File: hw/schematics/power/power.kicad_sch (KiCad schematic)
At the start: 16 parts

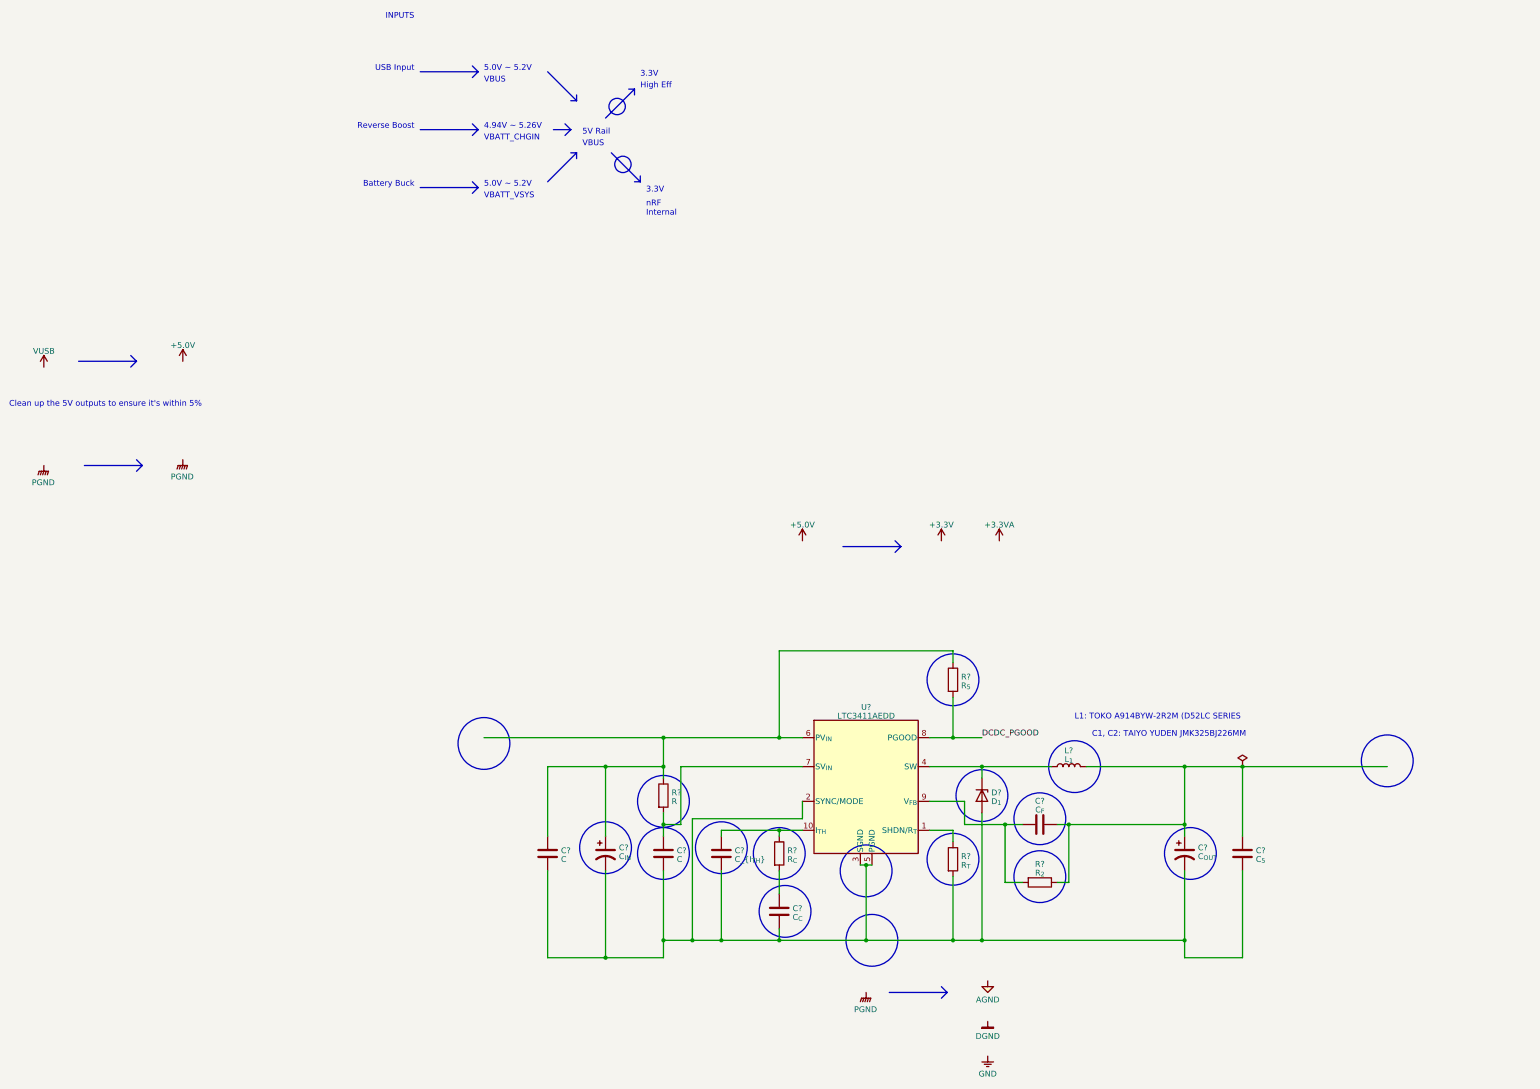
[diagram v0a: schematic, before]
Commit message: 
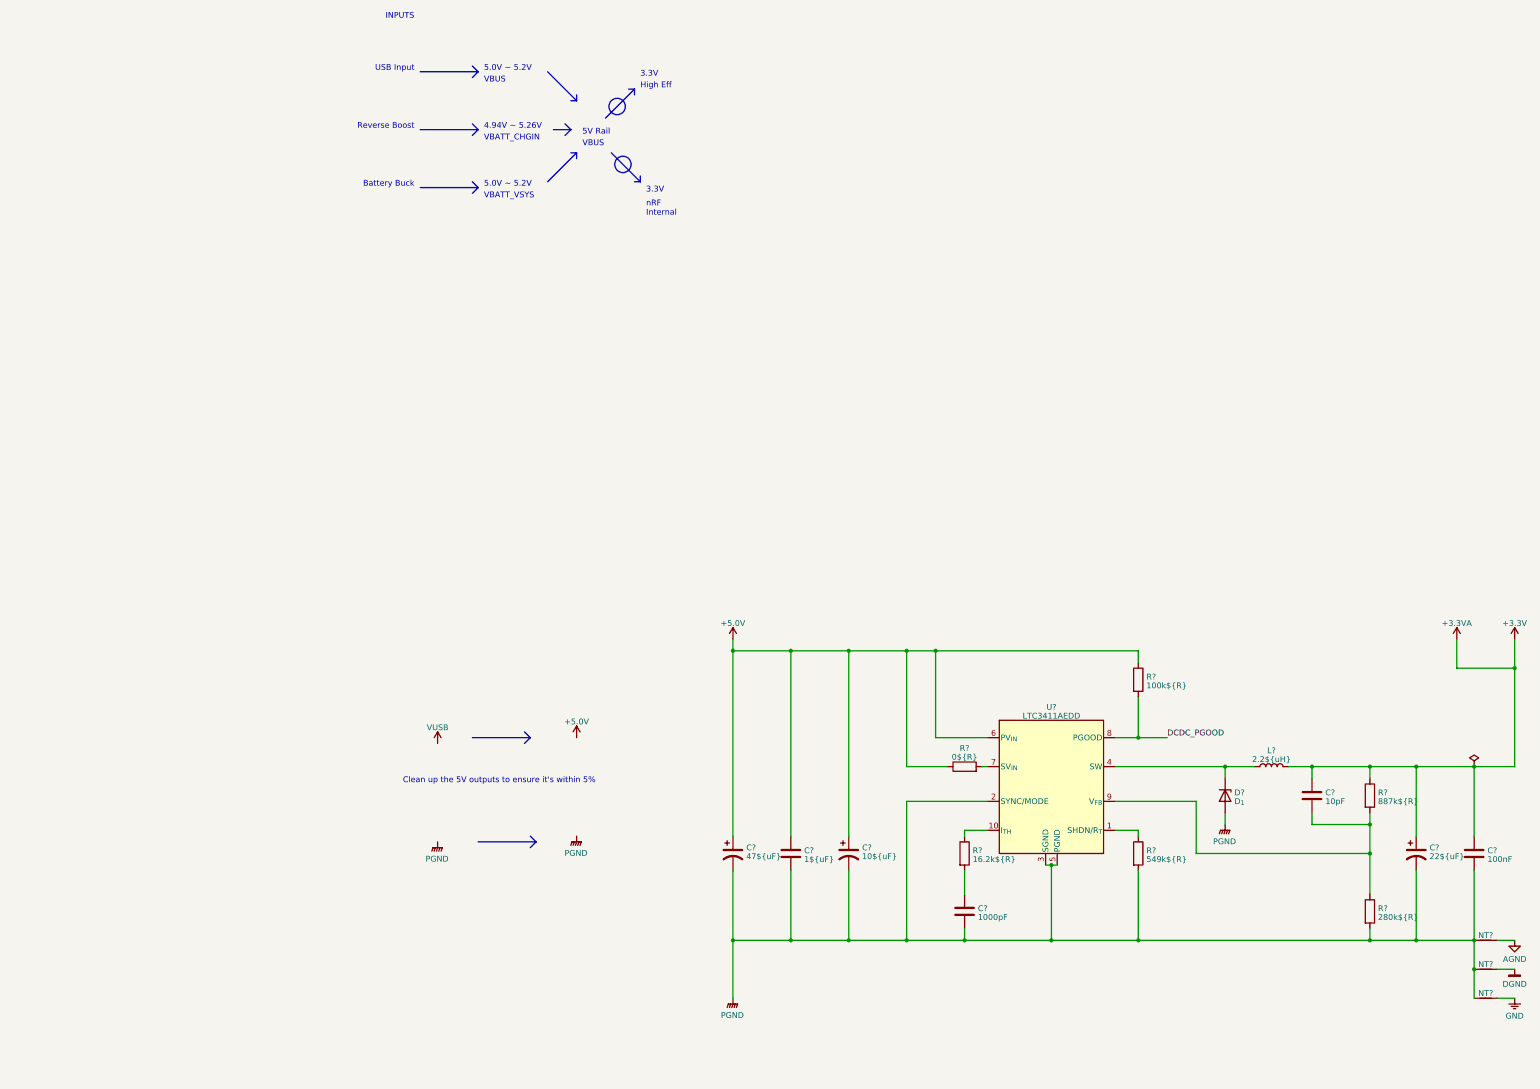
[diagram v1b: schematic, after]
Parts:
- removed C?: C_{OUT}, symbol Device:C_Polarized_US
- removed C?: C, symbol Device:C
- removed C?: C_{I_{TH}}, symbol Device:C
- added C?: 22${uF}, Capacitor_SMD:C_1206_3216Metric, symbol Device:C_Polarized_US
- added C?: 10${uF}, Capacitor_SMD:C_1206_3216Metric, symbol Device:C_Polarized_US
- added NT? (x3): NetTie_2, symbol Device:NetTie_2
- added R?: 280k${R}, symbol Device:R
- C?: value C_{5} -> 100nF; Digikey P/N (none) -> 478-7617-2-ND; Digikey URL (none) -> https://www.digikey.com.au/en/products/detail/kyocera-avx/0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; Mfr P/N (none) -> 0603YC104MAT
- C?: value C_{IN} -> 47${uF}; Digikey P/N (none) -> 478-9311-2-ND; Digikey URL (none) -> https://www.digikey.com.au/en/products/detail/kyocera-avx/T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; Mfr P/N (none) -> TRJC476K016RRJ
- C?: value C_{F} -> 10pF; footprint (none) -> Capacitor_SMD:C_0402_1005Metric; Digikey P/N (none) -> 478-12631-2-ND; Digikey URL (none) -> https://www.digikey.in/en/products/detail/kyocera-avx/04025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; Mfr P/N (none) -> 04025A100KAT2A
- C?: value C -> 1${uF}
- C?: value C_{C} -> 1000pF
- D?: footprint (none) -> Diode_SMD:D_SMA
- L?: value L_{1} -> 2.2${uH}
- R?: value R_{2} -> 887k${R}; Mfr P/N (none) -> CRCW0402887KFKED
- R?: value R_{T} -> 549k${R}
- R?: value R_{C} -> 16.2k${R}
- R?: value R -> 0${R}
- R?: value R_{5} -> 100k${R}
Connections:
- net +3.3V: now also C?.1, C?.2, L?.2, R?.1, C?.1
- net +5.0V: now also C?.1, C?.1, R?.1, R?.1, U?.6 (PV_{IN}), C?.1
- net AGND: now also NT?.2
- net DGND: now also NT?.2
- net GND: now also NT?.2
- net PGND: now also C?.2, C?.2, C?.2, C?.2, D?.2 (A), R?.2, U?.2 (SYNC/MODE), U?.3 (SGND), U?.5 (PGND), C?.2, C?.2, NT?.1, NT?.1, NT?.1, R?.2
- net at C?.1, R?.2, U?.9 (V_{FB}): now also R?.1
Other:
- note removed: "C1, C2: TAIYO YUDEN JMK325BJ226MM"
- note removed: "L1: TOKO A914BYW-2R2M (D52LC SERIES"
- moved on the sheet: C?, D?, L?, R?, U?

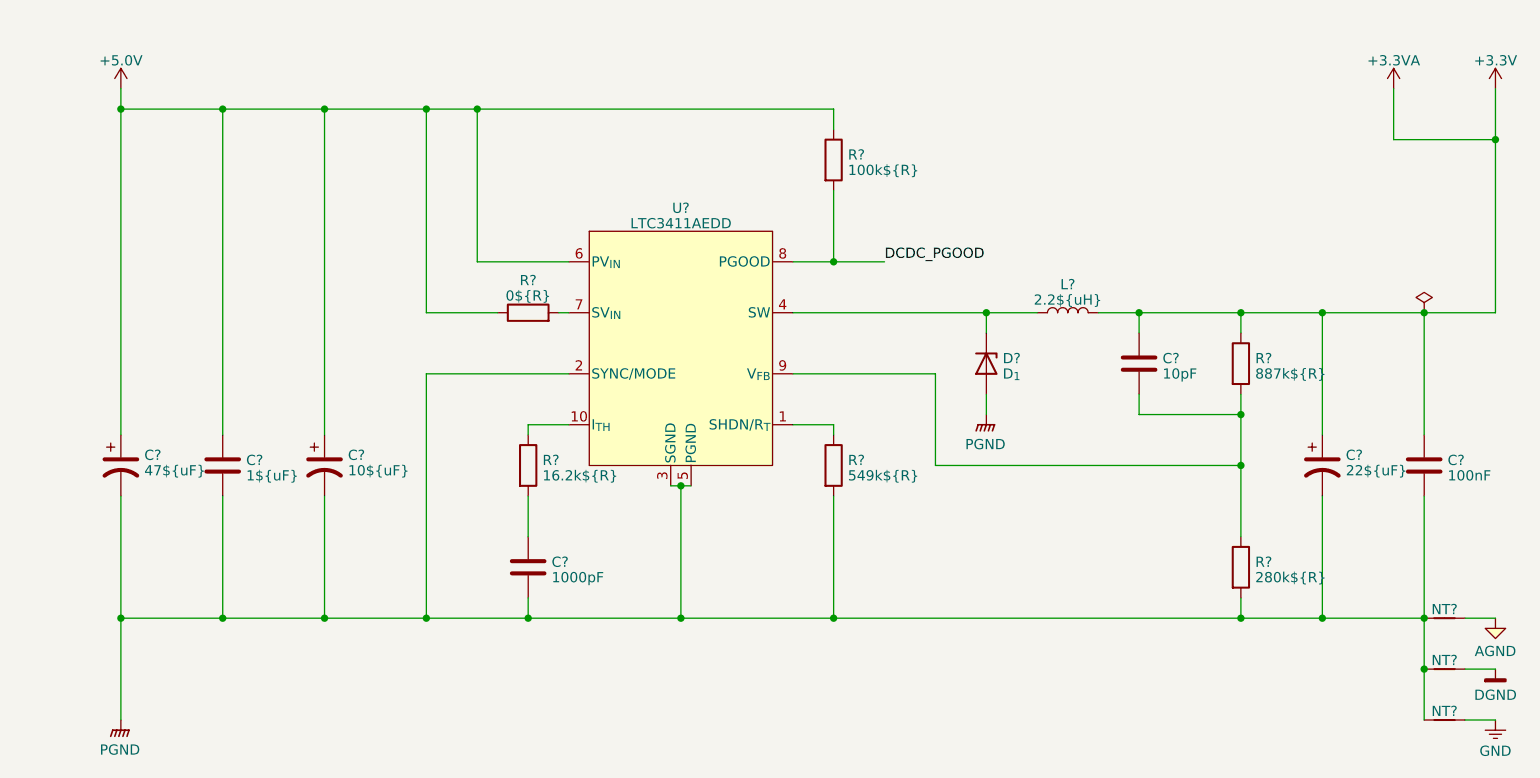
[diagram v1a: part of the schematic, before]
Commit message: 
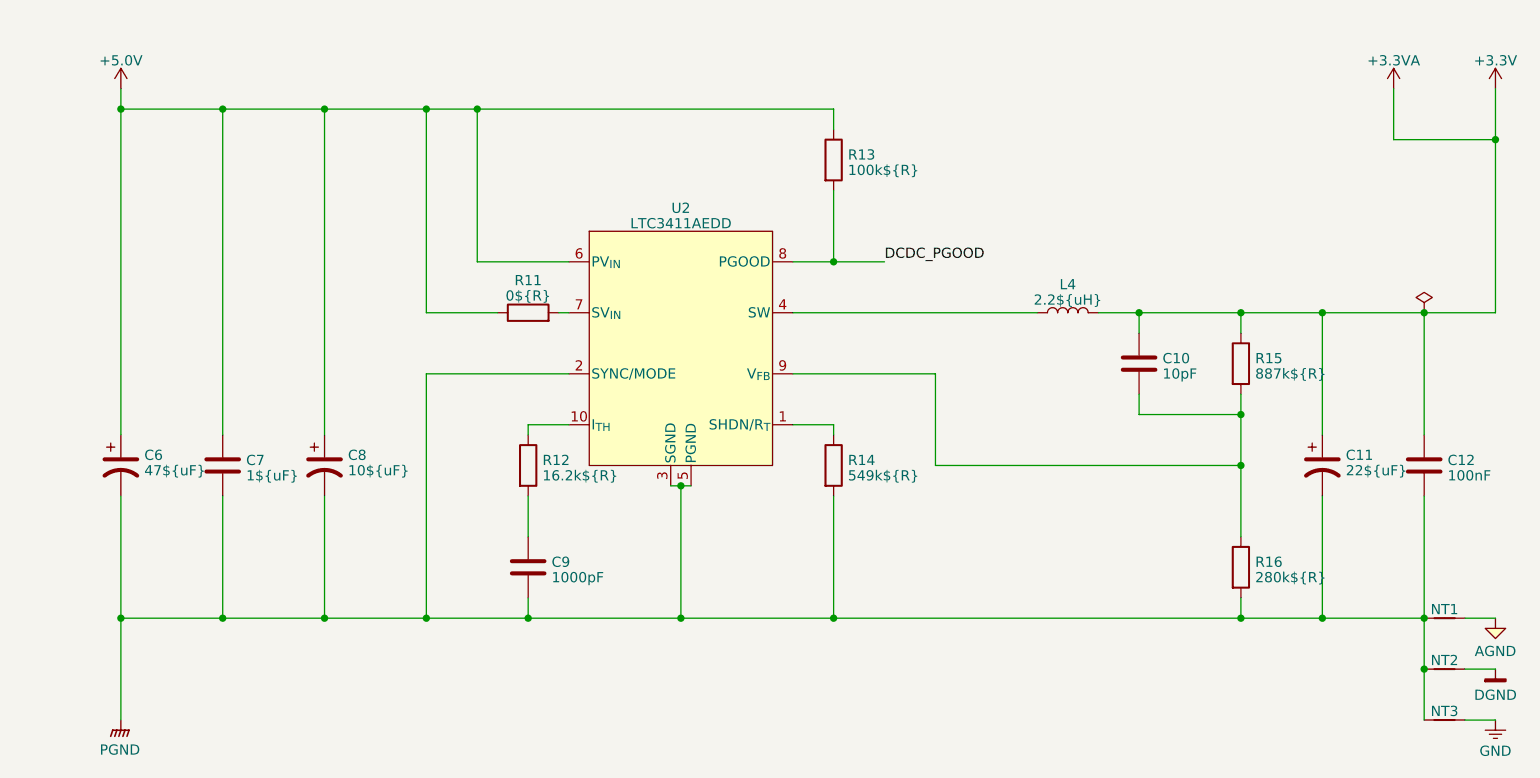
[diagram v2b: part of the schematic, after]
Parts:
- removed D?: D_{1}, Diode_SMD:D_SMA, symbol Device:D_Zener
- gave numbers to parts that had none: 18
